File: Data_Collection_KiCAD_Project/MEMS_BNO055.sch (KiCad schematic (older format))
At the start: 6 parts

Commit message: Fixed Component Libraries
Changed over from project specific to global libraries.
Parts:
- C? (x4): symbol Data_Collection_KiCAD_Project-rescue:C_Small-Device -> Data_Collection_KiCAD_Project-rescue:C_Small-Device-Data_Collection_KiCAD_Project-rescue
- U?: symbol Data_Collection_KiCAD_Project-rescue:BNO055-Sensor_Motion -> Data_Collection_KiCAD_Project-rescue:BNO055-Sensor_Motion-Data_Collection_KiCAD_Project-rescue
- Y?: symbol Data_Collection_KiCAD_Project-rescue:Crystal_Small-Device -> Data_Collection_KiCAD_Project-rescue:Crystal_Small-Device-Data_Collection_KiCAD_Project-rescue
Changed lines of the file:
@@
 $Descr A4 11693 8268
 encoding utf-8
-Sheet 8 10
+Sheet 8 9
 Title "ICM-20948 MEMS Chip"
 Date "2021-10-01"
@@
 $EndDescr
 $Comp
-L Data_Collection_KiCAD_Project-rescue:BNO055-Sensor_Motion U?
+L Data_Collection_KiCAD_Project-rescue:BNO055-Sensor_Motion-Data_Collection_KiCAD_Project-rescue U?
 U 1 1 61663BA8
 P 5650 3550
+AR Path="/61663BA8" Ref="U?"  Part="1"
+AR Path="/615A5159/61663BA8" Ref="U?"  Part="1"
 F 0 "U?" H 5650 4600 50  0000 C CNN
 F 1 "BNO055" H 5650 4500 50  0000 C CNN
@@
 	5750 2700 5550 2700
 $Comp
-L Data_Collection_KiCAD_Project-rescue:+3.3V-power #PWR?
+L Data_Collection_KiCAD_Project-rescue:+3.3V-power-Data_Collection_KiCAD_Project-rescue #PWR?
 U 1 1 6166AFE6
 P 5200 2700
+AR Path="/6166AFE6" Ref="#PWR?"  Part="1"
+AR Path="/615A5159/6166AFE6" Ref="#PWR?"  Part="1"
 F 0 "#PWR?" H 5200 2550 50  0001 C CNN
 F 1 "+3.3V" H 5215 2873 50  0000 C CNN
@@
 Connection ~ 5550 2700
 $Comp
-L Data_Collection_KiCAD_Project-rescue:GND-power #PWR?
+L Data_Collection_KiCAD_Project-rescue:GND-power-Data_Collection_KiCAD_Project-rescue #PWR?
 U 1 1 6166C199
 P 6400 2750
@@
 $EndComp
 $Comp
-L Data_Collection_KiCAD_Project-rescue:GND-power #PWR?
+L Data_Collection_KiCAD_Project-rescue:GND-power-Data_Collection_KiCAD_Project-rescue #PWR?
 U 1 1 6166D1D4
 P 5550 4350
@@
 ~BNO055_BTL
 $Comp
-L Data_Collection_KiCAD_Project-rescue:Crystal_Small-Device Y?
+L Data_Collection_KiCAD_Project-rescue:Crystal_Small-Device-Data_Collection_KiCAD_Project-rescue Y?
 U 1 1 6166FF64
 P 6450 3300
@@
 $EndComp
 $Comp
-L Data_Collection_KiCAD_Project-rescue:C_Small-Device C?
+L Data_Collection_KiCAD_Project-rescue:C_Small-Device-Data_Collection_KiCAD_Project-rescue C?
 U 1 1 6167196C
 P 6300 2700
+AR Path="/6167196C" Ref="C?"  Part="1"
+AR Path="/615A5159/6167196C" Ref="C?"  Part="1"
 F 0 "C?" V 6071 2700 50  0000 C CNN
 F 1 "0.1uF" V 6162 2700 50  0000 C CNN
@@
 	6450 3050 6450 3200
 $Comp
-L Data_Collection_KiCAD_Project-rescue:C_Small-Device C?
+L Data_Collection_KiCAD_Project-rescue:C_Small-Device-Data_Collection_KiCAD_Project-rescue C?
 U 1 1 6167A718
 P 6750 3050
+AR Path="/6167A718" Ref="C?"  Part="1"
+AR Path="/615A5159/6167A718" Ref="C?"  Part="1"
 F 0 "C?" V 6521 3050 50  0000 C CNN
 F 1 "0.1uF" V 6612 3050 50  0000 C CNN
@@
 $EndComp
 $Comp
-L Data_Collection_KiCAD_Project-rescue:C_Small-Device C?
+L Data_Collection_KiCAD_Project-rescue:C_Small-Device-Data_Collection_KiCAD_Project-rescue C?
 U 1 1 6167C82F
 P 6750 3550
+AR Path="/6167C82F" Ref="C?"  Part="1"
+AR Path="/615A5159/6167C82F" Ref="C?"  Part="1"
 F 0 "C?" V 6850 3550 50  0000 C CNN
 F 1 "0.1uF" V 6950 3550 50  0000 C CNN
@@
 Connection ~ 6450 3050
 $Comp
-L Data_Collection_KiCAD_Project-rescue:GND-power #PWR?
+L Data_Collection_KiCAD_Project-rescue:GND-power-Data_Collection_KiCAD_Project-rescue #PWR?
 U 1 1 6167EB61
 P 7100 3550
@@
 SCL
 $Comp
-L Data_Collection_KiCAD_Project-rescue:GND-power #PWR?
+L Data_Collection_KiCAD_Project-rescue:GND-power-Data_Collection_KiCAD_Project-rescue #PWR?
 U 1 1 61681CEA
 P 4850 4100
@@
 BNO055_INT
 $Comp
-L Data_Collection_KiCAD_Project-rescue:GND-power #PWR?
+L Data_Collection_KiCAD_Project-rescue:GND-power-Data_Collection_KiCAD_Project-rescue #PWR?
 U 1 1 616939D5
 P 6700 4350
@@
 $EndComp
 $Comp
-L Data_Collection_KiCAD_Project-rescue:C_Small-Device C?
+L Data_Collection_KiCAD_Project-rescue:C_Small-Device-Data_Collection_KiCAD_Project-rescue C?
 U 1 1 616964F3
 P 6450 4050
+AR Path="/616964F3" Ref="C?"  Part="1"
+AR Path="/615A5159/616964F3" Ref="C?"  Part="1"
 F 0 "C?" V 6550 4050 50  0000 C CNN
 F 1 "0.1uF" V 6650 4050 50  0000 C CNN

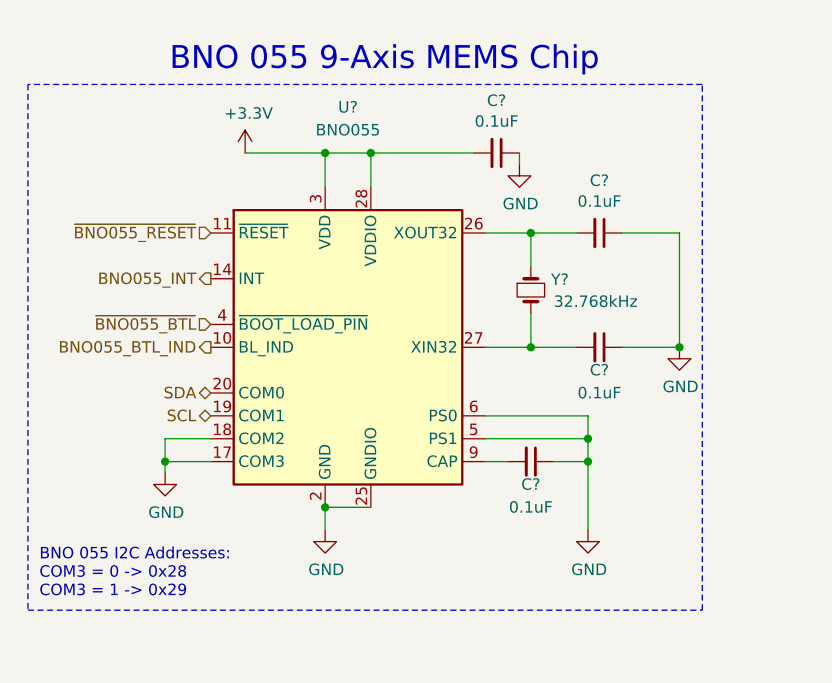
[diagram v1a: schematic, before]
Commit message: footprint and value changes
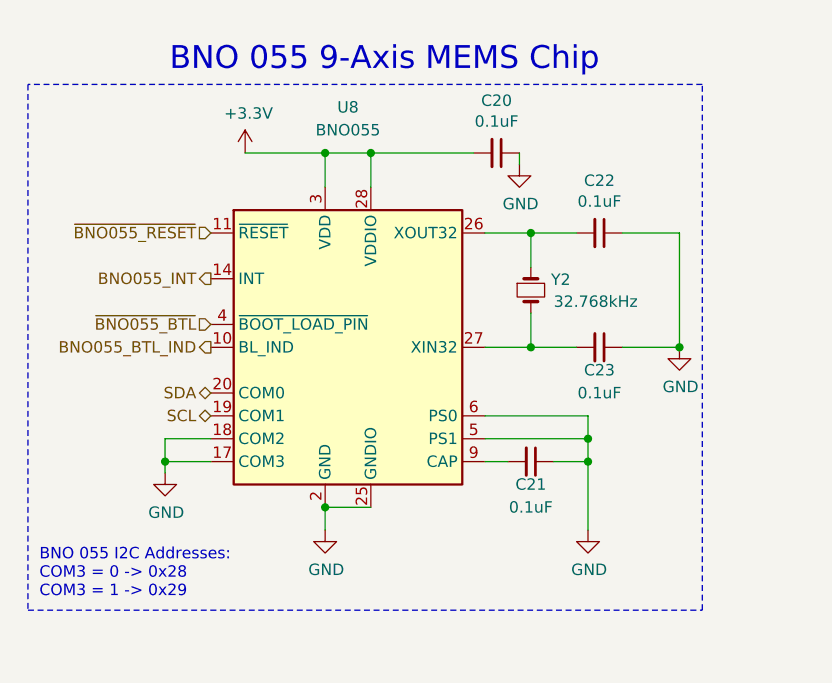
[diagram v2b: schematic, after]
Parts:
- C20, C21, C22, C23: renamed from C?; footprint (none) -> Capacitor_SMD:C_0603_1608Metric
- gave numbers to parts that had none: 2
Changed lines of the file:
@@
 P 5650 3550
 AR Path="/61663BA8" Ref="U?"  Part="1"
-AR Path="/615A5159/61663BA8" Ref="U?"  Part="1"
-F 0 "U?" H 5650 4600 50  0000 C CNN
+AR Path="/615A5159/61663BA8" Ref="U8"  Part="1"
+F 0 "U8" H 5650 4600 50  0000 C CNN
 F 1 "BNO055" H 5650 4500 50  0000 C CNN
 F 2 "Package_LGA:LGA-28_5.2x3.8mm_P0.5mm" H 5900 2900 50  0001 L CNN
@@
 P 5200 2700
 AR Path="/6166AFE6" Ref="#PWR?"  Part="1"
-AR Path="/615A5159/6166AFE6" Ref="#PWR?"  Part="1"
-F 0 "#PWR?" H 5200 2550 50  0001 C CNN
+AR Path="/615A5159/6166AFE6" Ref="#PWR049"  Part="1"
+F 0 "#PWR049" H 5200 2550 50  0001 C CNN
 F 1 "+3.3V" H 5215 2873 50  0000 C CNN
 F 2 "" H 5200 2700 50  0001 C CNN
@@
 Connection ~ 5550 2700
 $Comp
-L Data_Collection_KiCAD_Project-rescue:GND-power-Data_Collection_KiCAD_Project-rescue #PWR?
+L Data_Collection_KiCAD_Project-rescue:GND-power-Data_Collection_KiCAD_Project-rescue #PWR051
 U 1 1 6166C199
 P 6400 2750
-F 0 "#PWR?" H 6400 2500 50  0001 C CNN
+F 0 "#PWR051" H 6400 2500 50  0001 C CNN
 F 1 "GND" H 6405 2577 50  0000 C CNN
 F 2 "" H 6400 2750 50  0001 C CNN
@@
 $EndComp
 $Comp
-L Data_Collection_KiCAD_Project-rescue:GND-power-Data_Collection_KiCAD_Project-rescue #PWR?
+L Data_Collection_KiCAD_Project-rescue:GND-power-Data_Collection_KiCAD_Project-rescue #PWR050
 U 1 1 6166D1D4
 P 5550 4350
-F 0 "#PWR?" H 5550 4100 50  0001 C CNN
+F 0 "#PWR050" H 5550 4100 50  0001 C CNN
 F 1 "GND" H 5555 4177 50  0000 C CNN
 F 2 "" H 5550 4350 50  0001 C CNN
@@
 ~BNO055_BTL
 $Comp
-L Data_Collection_KiCAD_Project-rescue:Crystal_Small-Device-Data_Collection_KiCAD_Project-rescue Y?
+L Data_Collection_KiCAD_Project-rescue:Crystal_Small-Device-Data_Collection_KiCAD_Project-rescue Y2
 U 1 1 6166FF64
 P 6450 3300
-F 0 "Y?" V 6404 3388 50  0000 L CNN
+F 0 "Y2" V 6404 3388 50  0000 L CNN
 F 1 "32.768kHz" V 6500 3400 50  0000 L CNN
 F 2 "" H 6450 3300 50  0001 C CNN
@@
 P 6300 2700
 AR Path="/6167196C" Ref="C?"  Part="1"
-AR Path="/615A5159/6167196C" Ref="C?"  Part="1"
-F 0 "C?" V 6071 2700 50  0000 C CNN
+AR Path="/615A5159/6167196C" Ref="C20"  Part="1"
+F 0 "C20" V 6071 2700 50  0000 C CNN
 F 1 "0.1uF" V 6162 2700 50  0000 C CNN
-F 2 "" H 6300 2700 50  0001 C CNN
+F 2 "Capacitor_SMD:C_0603_1608Metric" H 6300 2700 50  0001 C CNN
 F 3 "~" H 6300 2700 50  0001 C CNN
 	1    6300 2700
@@
 P 6750 3050
 AR Path="/6167A718" Ref="C?"  Part="1"
-AR Path="/615A5159/6167A718" Ref="C?"  Part="1"
-F 0 "C?" V 6521 3050 50  0000 C CNN
+AR Path="/615A5159/6167A718" Ref="C22"  Part="1"
+F 0 "C22" V 6521 3050 50  0000 C CNN
 F 1 "0.1uF" V 6612 3050 50  0000 C CNN
-F 2 "" H 6750 3050 50  0001 C CNN
+F 2 "Capacitor_SMD:C_0603_1608Metric" H 6750 3050 50  0001 C CNN
 F 3 "~" H 6750 3050 50  0001 C CNN
 	1    6750 3050
@@
 P 6750 3550
 AR Path="/6167C82F" Ref="C?"  Part="1"
-AR Path="/615A5159/6167C82F" Ref="C?"  Part="1"
-F 0 "C?" V 6850 3550 50  0000 C CNN
+AR Path="/615A5159/6167C82F" Ref="C23"  Part="1"
+F 0 "C23" V 6850 3550 50  0000 C CNN
 F 1 "0.1uF" V 6950 3550 50  0000 C CNN
-F 2 "" H 6750 3550 50  0001 C CNN
+F 2 "Capacitor_SMD:C_0603_1608Metric" H 6750 3550 50  0001 C CNN
 F 3 "~" H 6750 3550 50  0001 C CNN
 	1    6750 3550
@@
 Connection ~ 6450 3050
 $Comp
-L Data_Collection_KiCAD_Project-rescue:GND-power-Data_Collection_KiCAD_Project-rescue #PWR?
+L Data_Collection_KiCAD_Project-rescue:GND-power-Data_Collection_KiCAD_Project-rescue #PWR053
 U 1 1 6167EB61
 P 7100 3550
-F 0 "#PWR?" H 7100 3300 50  0001 C CNN
+F 0 "#PWR053" H 7100 3300 50  0001 C CNN
 F 1 "GND" H 7105 3377 50  0000 C CNN
 F 2 "" H 7100 3550 50  0001 C CNN
@@
 SCL
 $Comp
-L Data_Collection_KiCAD_Project-rescue:GND-power-Data_Collection_KiCAD_Project-rescue #PWR?
+L Data_Collection_KiCAD_Project-rescue:GND-power-Data_Collection_KiCAD_Project-rescue #PWR048
 U 1 1 61681CEA
 P 4850 4100
-F 0 "#PWR?" H 4850 3850 50  0001 C CNN
+F 0 "#PWR048" H 4850 3850 50  0001 C CNN
 F 1 "GND" H 4855 3927 50  0000 C CNN
 F 2 "" H 4850 4100 50  0001 C CNN
@@
 BNO055_INT
 $Comp
-L Data_Collection_KiCAD_Project-rescue:GND-power-Data_Collection_KiCAD_Project-rescue #PWR?
+L Data_Collection_KiCAD_Project-rescue:GND-power-Data_Collection_KiCAD_Project-rescue #PWR052
 U 1 1 616939D5
 P 6700 4350
-F 0 "#PWR?" H 6700 4100 50  0001 C CNN
+F 0 "#PWR052" H 6700 4100 50  0001 C CNN
 F 1 "GND" H 6705 4177 50  0000 C CNN
 F 2 "" H 6700 4350 50  0001 C CNN
@@
 P 6450 4050
 AR Path="/616964F3" Ref="C?"  Part="1"
-AR Path="/615A5159/616964F3" Ref="C?"  Part="1"
-F 0 "C?" V 6550 4050 50  0000 C CNN
+AR Path="/615A5159/616964F3" Ref="C21"  Part="1"
+F 0 "C21" V 6550 4050 50  0000 C CNN
 F 1 "0.1uF" V 6650 4050 50  0000 C CNN
-F 2 "" H 6450 4050 50  0001 C CNN
+F 2 "Capacitor_SMD:C_0603_1608Metric" H 6450 4050 50  0001 C CNN
 F 3 "~" H 6450 4050 50  0001 C CNN
 	1    6450 4050

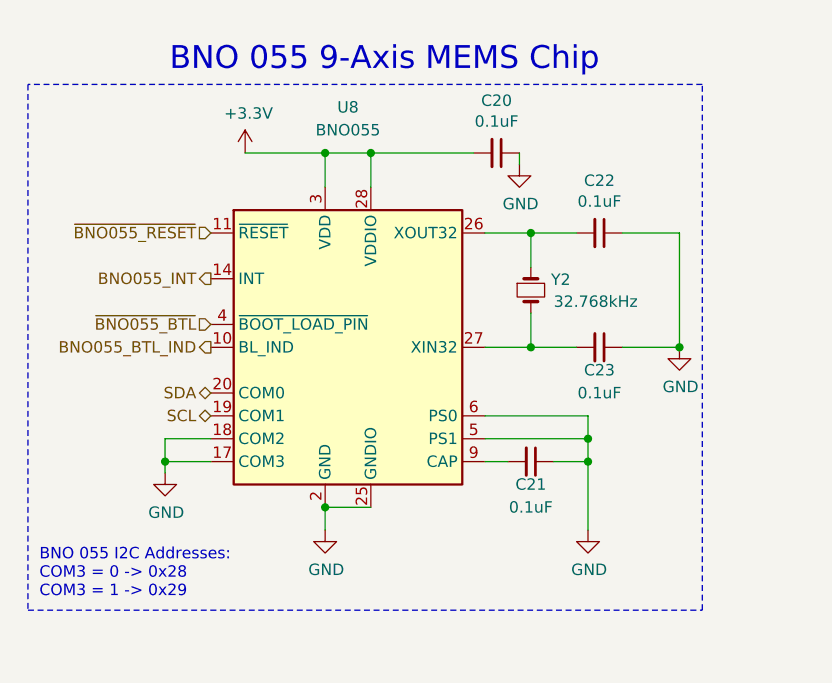
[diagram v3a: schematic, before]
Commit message: footprint changes
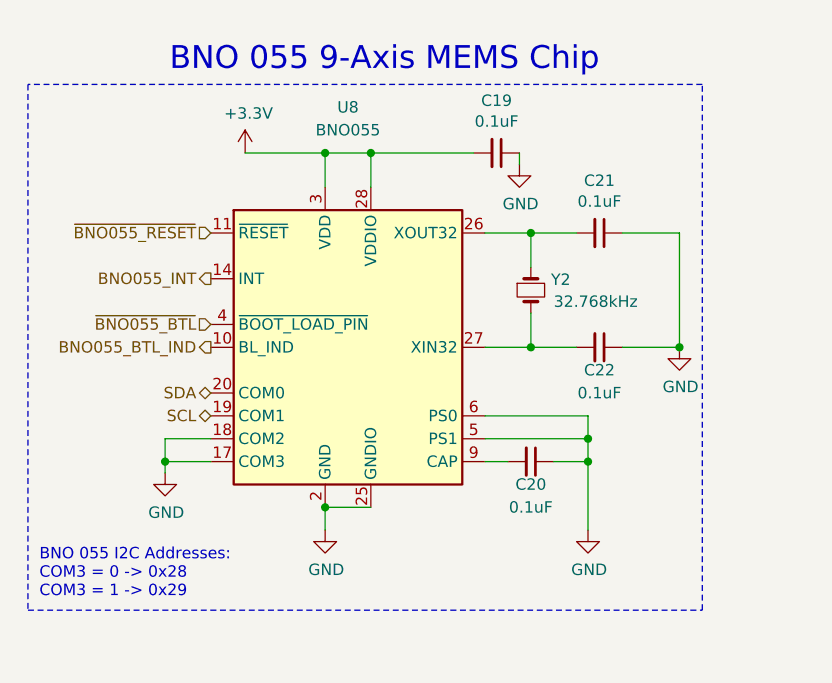
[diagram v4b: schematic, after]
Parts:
- renumbered C20 to C19, C21 to C20, C22 to C21, C23 to C22
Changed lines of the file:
@@
 P 5200 2700
 AR Path="/6166AFE6" Ref="#PWR?"  Part="1"
-AR Path="/615A5159/6166AFE6" Ref="#PWR049"  Part="1"
-F 0 "#PWR049" H 5200 2550 50  0001 C CNN
+AR Path="/615A5159/6166AFE6" Ref="#PWR042"  Part="1"
+F 0 "#PWR042" H 5200 2550 50  0001 C CNN
 F 1 "+3.3V" H 5215 2873 50  0000 C CNN
 F 2 "" H 5200 2700 50  0001 C CNN
@@
 Connection ~ 5550 2700
 $Comp
-L Data_Collection_KiCAD_Project-rescue:GND-power-Data_Collection_KiCAD_Project-rescue #PWR051
+L Data_Collection_KiCAD_Project-rescue:GND-power-Data_Collection_KiCAD_Project-rescue #PWR044
 U 1 1 6166C199
 P 6400 2750
-F 0 "#PWR051" H 6400 2500 50  0001 C CNN
+F 0 "#PWR044" H 6400 2500 50  0001 C CNN
 F 1 "GND" H 6405 2577 50  0000 C CNN
 F 2 "" H 6400 2750 50  0001 C CNN
@@
 $EndComp
 $Comp
-L Data_Collection_KiCAD_Project-rescue:GND-power-Data_Collection_KiCAD_Project-rescue #PWR050
+L Data_Collection_KiCAD_Project-rescue:GND-power-Data_Collection_KiCAD_Project-rescue #PWR043
 U 1 1 6166D1D4
 P 5550 4350
-F 0 "#PWR050" H 5550 4100 50  0001 C CNN
+F 0 "#PWR043" H 5550 4100 50  0001 C CNN
 F 1 "GND" H 5555 4177 50  0000 C CNN
 F 2 "" H 5550 4350 50  0001 C CNN
@@
 P 6300 2700
 AR Path="/6167196C" Ref="C?"  Part="1"
-AR Path="/615A5159/6167196C" Ref="C20"  Part="1"
-F 0 "C20" V 6071 2700 50  0000 C CNN
+AR Path="/615A5159/6167196C" Ref="C19"  Part="1"
+F 0 "C19" V 6071 2700 50  0000 C CNN
 F 1 "0.1uF" V 6162 2700 50  0000 C CNN
 F 2 "Capacitor_SMD:C_0603_1608Metric" H 6300 2700 50  0001 C CNN
@@
 P 6750 3050
 AR Path="/6167A718" Ref="C?"  Part="1"
-AR Path="/615A5159/6167A718" Ref="C22"  Part="1"
-F 0 "C22" V 6521 3050 50  0000 C CNN
+AR Path="/615A5159/6167A718" Ref="C21"  Part="1"
+F 0 "C21" V 6521 3050 50  0000 C CNN
 F 1 "0.1uF" V 6612 3050 50  0000 C CNN
 F 2 "Capacitor_SMD:C_0603_1608Metric" H 6750 3050 50  0001 C CNN
@@
 P 6750 3550
 AR Path="/6167C82F" Ref="C?"  Part="1"
-AR Path="/615A5159/6167C82F" Ref="C23"  Part="1"
-F 0 "C23" V 6850 3550 50  0000 C CNN
+AR Path="/615A5159/6167C82F" Ref="C22"  Part="1"
+F 0 "C22" V 6850 3550 50  0000 C CNN
 F 1 "0.1uF" V 6950 3550 50  0000 C CNN
 F 2 "Capacitor_SMD:C_0603_1608Metric" H 6750 3550 50  0001 C CNN
@@
 Connection ~ 6450 3050
 $Comp
-L Data_Collection_KiCAD_Project-rescue:GND-power-Data_Collection_KiCAD_Project-rescue #PWR053
+L Data_Collection_KiCAD_Project-rescue:GND-power-Data_Collection_KiCAD_Project-rescue #PWR046
 U 1 1 6167EB61
 P 7100 3550
-F 0 "#PWR053" H 7100 3300 50  0001 C CNN
+F 0 "#PWR046" H 7100 3300 50  0001 C CNN
 F 1 "GND" H 7105 3377 50  0000 C CNN
 F 2 "" H 7100 3550 50  0001 C CNN
@@
 SCL
 $Comp
-L Data_Collection_KiCAD_Project-rescue:GND-power-Data_Collection_KiCAD_Project-rescue #PWR048
+L Data_Collection_KiCAD_Project-rescue:GND-power-Data_Collection_KiCAD_Project-rescue #PWR041
 U 1 1 61681CEA
 P 4850 4100
-F 0 "#PWR048" H 4850 3850 50  0001 C CNN
+F 0 "#PWR041" H 4850 3850 50  0001 C CNN
 F 1 "GND" H 4855 3927 50  0000 C CNN
 F 2 "" H 4850 4100 50  0001 C CNN
@@
 BNO055_INT
 $Comp
-L Data_Collection_KiCAD_Project-rescue:GND-power-Data_Collection_KiCAD_Project-rescue #PWR052
+L Data_Collection_KiCAD_Project-rescue:GND-power-Data_Collection_KiCAD_Project-rescue #PWR045
 U 1 1 616939D5
 P 6700 4350
-F 0 "#PWR052" H 6700 4100 50  0001 C CNN
+F 0 "#PWR045" H 6700 4100 50  0001 C CNN
 F 1 "GND" H 6705 4177 50  0000 C CNN
 F 2 "" H 6700 4350 50  0001 C CNN
@@
 P 6450 4050
 AR Path="/616964F3" Ref="C?"  Part="1"
-AR Path="/615A5159/616964F3" Ref="C21"  Part="1"
-F 0 "C21" V 6550 4050 50  0000 C CNN
+AR Path="/615A5159/616964F3" Ref="C20"  Part="1"
+F 0 "C20" V 6550 4050 50  0000 C CNN
 F 1 "0.1uF" V 6650 4050 50  0000 C CNN
 F 2 "Capacitor_SMD:C_0603_1608Metric" H 6450 4050 50  0001 C CNN

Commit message: Finalized Schematic
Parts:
- Y2: footprint (none) -> Crystal:Crystal_DS26_D2.0mm_L6.0mm_Horizontal_1EP_style2
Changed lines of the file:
@@
 F 0 "Y2" V 6404 3388 50  0000 L CNN
 F 1 "32.768kHz" V 6500 3400 50  0000 L CNN
-F 2 "" H 6450 3300 50  0001 C CNN
+F 2 "Crystal:Crystal_DS26_D2.0mm_L6.0mm_Horizontal_1EP_style2" H 6450 3300 50  0001 C CNN
 F 3 "~" H 6450 3300 50  0001 C CNN
 	1    6450 3300
